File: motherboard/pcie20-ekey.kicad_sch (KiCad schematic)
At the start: 6 parts, among them J13 Bus_M.2_Socket_E

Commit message: synchronizing hierarchical pins
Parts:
- C33, C34: footprint (none) -> Capacitor_SMD:C_0402_1005Metric
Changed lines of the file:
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@@
 			)
 		)
-		(property "Footprint" ""
+		(property "Footprint" "Capacitor_SMD:C_0402_1005Metric"
 			(at 114.3 77.47 0)
 			(effects
@@
 		(pin "1"
 		)
+		(instances
+			(project ""
+				(path "/025fe4d1-0305-4b34-be04-f8d9818125a4/4296e3bb-d60d-4db1-b6b7-692bdef698b7"
+					(reference "#PWR072")
+					(unit 1)
+				)
+			)
+		)
 	)
 	(symbol
@@
 			)
 		)
-		(property "Footprint" ""
+		(property "Footprint" "Capacitor_SMD:C_0402_1005Metric"
 			(at 107.95 74.93 0)
 			(effects

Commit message: linked all footprints
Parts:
- J13: footprint (none) -> WIRELESS_E_KEY:CONN-SMD_APCI0147-P001A
- R50, R51, R52: footprint (none) -> Resistor_SMD:R_0402_1005Metric
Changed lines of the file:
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@@
 			)
 		)
-		(property "Footprint" ""
+		(property "Footprint" "Resistor_SMD:R_0402_1005Metric"
 			(at 111.76 138.43 0)
 			(effects
@@
 			)
 		)
-		(property "Footprint" ""
+		(property "Footprint" "Resistor_SMD:R_0402_1005Metric"
 			(at 173.99 105.41 0)
 			(effects
@@
 			)
 		)
-		(property "Footprint" ""
+		(property "Footprint" "Resistor_SMD:R_0402_1005Metric"
 			(at 179.07 107.95 0)
 			(effects
@@
 			)
 		)
-		(property "Footprint" ""
+		(property "Footprint" "WIRELESS_E_KEY:CONN-SMD_APCI0147-P001A"
 			(at 144.78 81.28 0)
 			(effects

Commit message: work preparing for routing
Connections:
- no-connect marks 17 -> 23

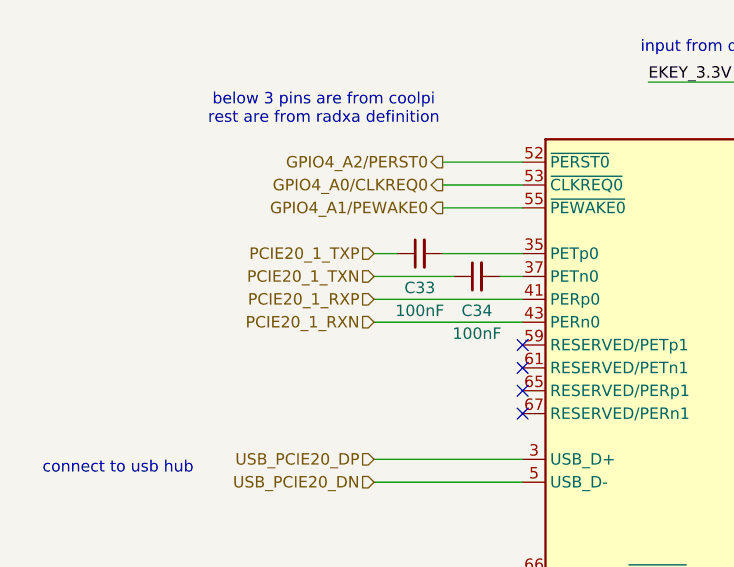
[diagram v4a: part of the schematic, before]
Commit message: placement roughly halfway done
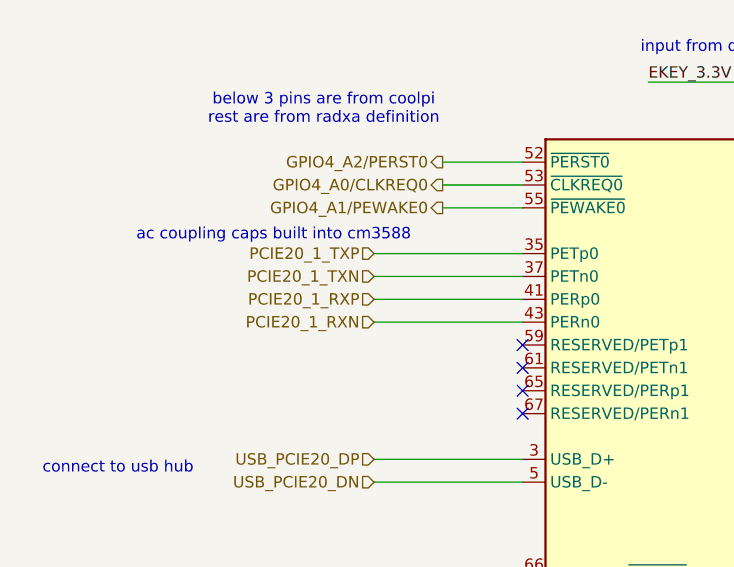
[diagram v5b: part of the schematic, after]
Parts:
- removed C33, C34: 100nF, Capacitor_SMD:C_0402_1005Metric, symbol Device:C_Small
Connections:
- net PCIE20_1_TXN: now also J13.37 (PETn0)
- net PCIE20_1_TXP: now also J13.35 (PETp0)
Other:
- note added: "ac coupling caps built into cm3588"
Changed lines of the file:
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@@
+		)
+	)
+	(text "ac coupling caps built into cm3588"
+		(exclude_from_sim no)
+		(at 76.454 72.898 0)
+		(effects
+			(font
+				(size 1.27 1.27)
+			)
+			(justify left)
 		)
 	)
@@
 	(wire
 		(pts
-			(xy 102.87 74.93) (xy 105.41 74.93)
+			(xy 102.87 74.93) (xy 119.38 74.93)
 		)
 		(stroke
@@
 	(wire
 		(pts
-			(xy 102.87 77.47) (xy 111.76 77.47)
+			(xy 102.87 77.47) (xy 119.38 77.47)
 		)
 		(stroke
@@
 	(wire
 		(pts
-			(xy 110.49 74.93) (xy 119.38 74.93)
-		)
-		(stroke
-			(width 0)
-			(type default)
-		)
-	)
-	(wire
-		(pts
 			(xy 102.87 146.05) (xy 119.38 146.05)
 		)
@@
 		(pts
 			(xy 114.3 138.43) (xy 119.38 138.43)
-		)
-		(stroke
-			(width 0)
-			(type default)
-		)
-	)
-	(wire
-		(pts
-			(xy 116.84 77.47) (xy 119.38 77.47)
 		)
 		(stroke
@@
 		)
 	)
-	(symbol
-		(lib_id "Device:C_Small")
-		(at 107.95 74.93 90)
-		(unit 1)
-		(exclude_from_sim no)
-		(in_bom yes)
-		(on_board yes)
-		(dnp no)
-		(fields_autoplaced yes)
-		(property "Reference" "C33"
-			(at 107.9563 78.74 90)
-			(effects
-				(font
-					(size 1.27 1.27)
-				)
-			)
-		)
-		(property "Value" "100nF"
-			(at 107.9563 81.28 90)
-			(effects
-				(font
-					(size 1.27 1.27)
-				)
-			)
-		)
-		(property "Footprint" "Capacitor_SMD:C_0402_1005Metric"
-			(at 107.95 74.93 0)
-			(effects
-				(font
-					(size 1.27 1.27)
-				)
-				(hide yes)
-			)
-		)
-		(property "Datasheet" "~"
-			(at 107.95 74.93 0)
-			(effects
-				(font
-					(size 1.27 1.27)
-				)
-				(hide yes)
-			)
-		)
-		(property "Description" "Unpolarized capacitor, small symbol"
-			(at 107.95 74.93 0)
-			(effects
-				(font
-					(size 1.27 1.27)
-				)
-				(hide yes)
-			)
-		)
-		(pin "1"
-		)
-		(pin "2"
-		)
-		(instances
-			(project "motherboard"
-				(path "/025fe4d1-0305-4b34-be04-f8d9818125a4/4296e3bb-d60d-4db1-b6b7-692bdef698b7"
-					(reference "C33")
-					(unit 1)
-				)
-			)
-		)
-	)
-	(symbol
-		(lib_id "Device:C_Small")
-		(at 114.3 77.47 90)
-		(unit 1)
-		(exclude_from_sim no)
-		(in_bom yes)
-		(on_board yes)
-		(dnp no)
-		(fields_autoplaced yes)
-		(property "Reference" "C34"
-			(at 114.3063 81.28 90)
-			(effects
-				(font
-					(size 1.27 1.27)
-				)
-			)
-		)
-		(property "Value" "100nF"
-			(at 114.3063 83.82 90)
-			(effects
-				(font
-					(size 1.27 1.27)
-				)
-			)
-		)
-		(property "Footprint" "Capacitor_SMD:C_0402_1005Metric"
-			(at 114.3 77.47 0)
-			(effects
-				(font
-					(size 1.27 1.27)
-				)
-				(hide yes)
-			)
-		)
-		(property "Datasheet" "~"
-			(at 114.3 77.47 0)
-			(effects
-				(font
-					(size 1.27 1.27)
-				)
-				(hide yes)
-			)
-		)
-		(property "Description" "Unpolarized capacitor, small symbol"
-			(at 114.3 77.47 0)
-			(effects
-				(font
-					(size 1.27 1.27)
-				)
-				(hide yes)
-			)
-		)
-		(pin "1"
-		)
-		(pin "2"
-		)
-		(instances
-			(project "motherboard"
-				(path "/025fe4d1-0305-4b34-be04-f8d9818125a4/4296e3bb-d60d-4db1-b6b7-692bdef698b7"
-					(reference "C34")
-					(unit 1)
-				)
-			)
-		)
-	)

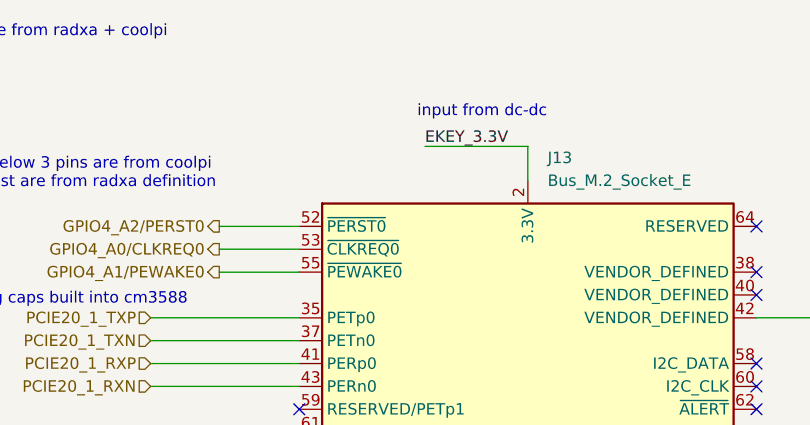
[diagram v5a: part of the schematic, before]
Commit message: added two more display eval test boards
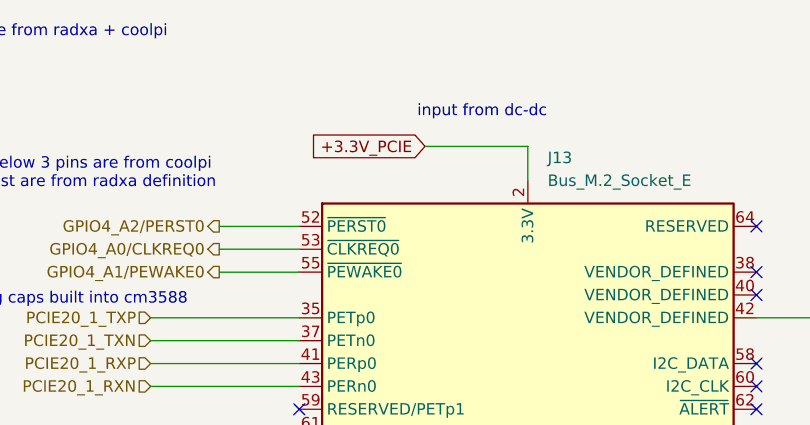
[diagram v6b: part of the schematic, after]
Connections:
- net EKEY_3.3V renamed +3.3V_PCIE
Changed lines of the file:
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@@
+	(wire
+		(pts
+			(xy 102.87 74.93) (xy 119.38 74.93)
+		)
+		(stroke
+			(width 0)
+			(type default)
+		)
+	)
+	(wire
+		(pts
+			(xy 176.53 107.95) (xy 170.18 107.95)
+		)
+		(stroke
+			(width 0)
+			(type default)
+		)
+	)
+	(wire
+		(pts
+			(xy 102.87 135.89) (xy 119.38 135.89)
+		)
+		(stroke
+			(width 0)
+			(type default)
+		)
+	)
 	(wire
 		(pts
@@
 	(wire
 		(pts
-			(xy 102.87 74.93) (xy 119.38 74.93)
-		)
-		(stroke
-			(width 0)
-			(type default)
-		)
-	)
-	(wire
-		(pts
-			(xy 176.53 107.95) (xy 170.18 107.95)
-		)
-		(stroke
-			(width 0)
-			(type default)
-		)
-	)
-	(wire
-		(pts
-			(xy 102.87 135.89) (xy 119.38 135.89)
-		)
-		(stroke
-			(width 0)
-			(type default)
-		)
-	)
-	(wire
-		(pts
 			(xy 144.78 55.88) (xy 144.78 59.69)
 		)
@@
 		)
 	)
-	(label "EKEY_3.3V"
-		(at 133.35 55.88 0)
+	(global_label "+3.3V_PCIE"
+		(shape input)
+		(at 133.35 55.88 180)
 		(fields_autoplaced yes)
 		(effects
@@
 				(size 1.27 1.27)
 			)
-			(justify left bottom)
-		)
-	)
+			(justify right)
+		)
+		(property "Intersheetrefs" "${INTERSHEET_REFS}"
+			(at 119.4186 55.88 0)
+			(effects
+				(font
+					(size 1.27 1.27)
+				)
+				(justify right)
+				(hide yes)
+			)
+		)
+	)

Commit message: v0.2 75 routes left!
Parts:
- added C54, C55: 22uF, Capacitor_SMD:C_0603_1608Metric, symbol Device:C_Small
- added C78: 1uF, Capacitor_SMD:C_0402_1005Metric, symbol Device:C_Small
- added C79: 0.1uF, Capacitor_SMD:C_0402_1005Metric, symbol Device:C_Small
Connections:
- net +3.3V_PCIE: now also C54.1, C55.1, C78.1, C79.1
- net GND: now also C54.2, C55.2, C78.2, C79.2

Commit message: mainboard v0.3 + power WIP
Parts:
- removed C55: 22uF, Capacitor_SMD:C_0603_1608Metric, symbol Device:C_Small
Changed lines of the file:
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@@
 	(title_block
 		(title "anyon e")
-		(date "2024-06-12")
-		(rev "V0.1")
+		(date "2024-09-15")
+		(rev "V0.3")
 		(company "Byran Huang")
 		(comment 4 "Proof of concept board for feature verification")
@@
 	)
 	(junction
-		(at 104.14 46.99)
-		(diameter 0)
-		(color 0 0 0 0)
-	)
-	(junction
 		(at 114.3 52.07)
 		(diameter 0)
@@
 	)
 	(junction
-		(at 104.14 52.07)
-		(diameter 0)
-		(color 0 0 0 0)
-	)
-	(junction
 		(at 119.38 52.07)
 		(diameter 0)
@@
 	(wire
 		(pts
-			(xy 104.14 52.07) (xy 114.3 52.07)
+			(xy 99.06 52.07) (xy 114.3 52.07)
 		)
 		(stroke
@@
 	(wire
 		(pts
-			(xy 99.06 52.07) (xy 104.14 52.07)
-		)
-		(stroke
-			(width 0)
-			(type default)
-		)
-	)
-	(wire
-		(pts
 			(xy 119.38 52.07) (xy 123.19 52.07)
 		)
@@
 	(wire
 		(pts
-			(xy 99.06 46.99) (xy 104.14 46.99)
+			(xy 99.06 46.99) (xy 114.3 46.99)
 		)
 		(stroke
@@
 		(pts
 			(xy 102.87 100.33) (xy 119.38 100.33)
-		)
-		(stroke
-			(width 0)
-			(type default)
-		)
-	)
-	(wire
-		(pts
-			(xy 104.14 46.99) (xy 114.3 46.99)
 		)
 		(stroke
@@
 					(unit 1)
 				)
-			)
-		)
-	)
-	(symbol
-		(lib_id "Device:C_Small")
-		(at 104.14 49.53 0)
-		(unit 1)
-		(exclude_from_sim no)
-		(in_bom yes)
-		(on_board yes)
-		(dnp no)
-		(property "Reference" "C55"
-			(at 106.68 48.2662 0)
-			(effects
-				(font
-					(size 1.27 1.27)
-				)
-				(justify left)
-			)
-		)
-		(property "Value" "22uF"
-			(at 106.68 50.8062 0)
-			(effects
-				(font
-					(size 1.27 1.27)
-				)
-				(justify left)
-			)
-		)
-		(property "Footprint" "Capacitor_SMD:C_0603_1608Metric"
-			(at 104.14 49.53 0)
-			(effects
-				(font
-					(size 1.27 1.27)
-				)
-				(hide yes)
-			)
-		)
-		(property "Datasheet" "~"
-			(at 104.14 49.53 0)
-			(effects
-				(font
-					(size 1.27 1.27)
-				)
-				(hide yes)
-			)
-		)
-		(property "Description" "Unpolarized capacitor, small symbol"
-			(at 103.886 44.958 0)
-			(effects
-				(font
-					(size 1.27 1.27)
-					(italic yes)
-				)
-				(hide yes)
-			)
-		)
-		(pin "1"
-		)
-		(pin "2"
-		)
-		(instances
-			(project "motherboard"
-				(path "/025fe4d1-0305-4b34-be04-f8d9818125a4/4296e3bb-d60d-4db1-b6b7-692bdef698b7"
-					(reference "C55")
-					(unit 1)
-				)
